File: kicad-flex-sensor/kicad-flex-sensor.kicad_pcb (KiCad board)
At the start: 2 copper layers, 68.6 x 53.3 mm, 8 parts, among them J1 Power, J2 Digital/PWM, J3 Analog, J4 Digital/PWM

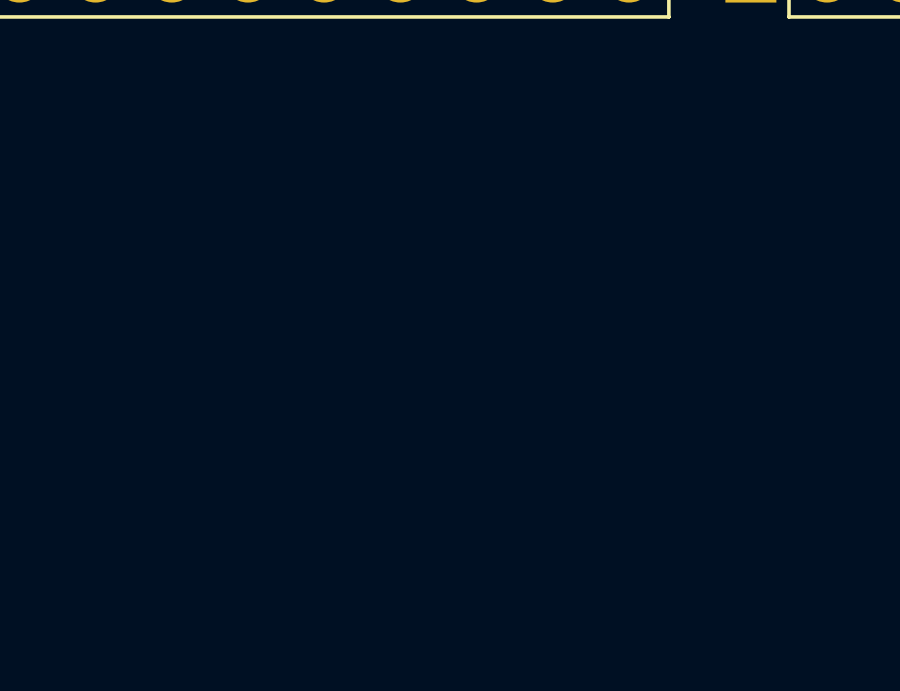
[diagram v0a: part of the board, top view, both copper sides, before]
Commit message: add bluetooth symbol and footprint
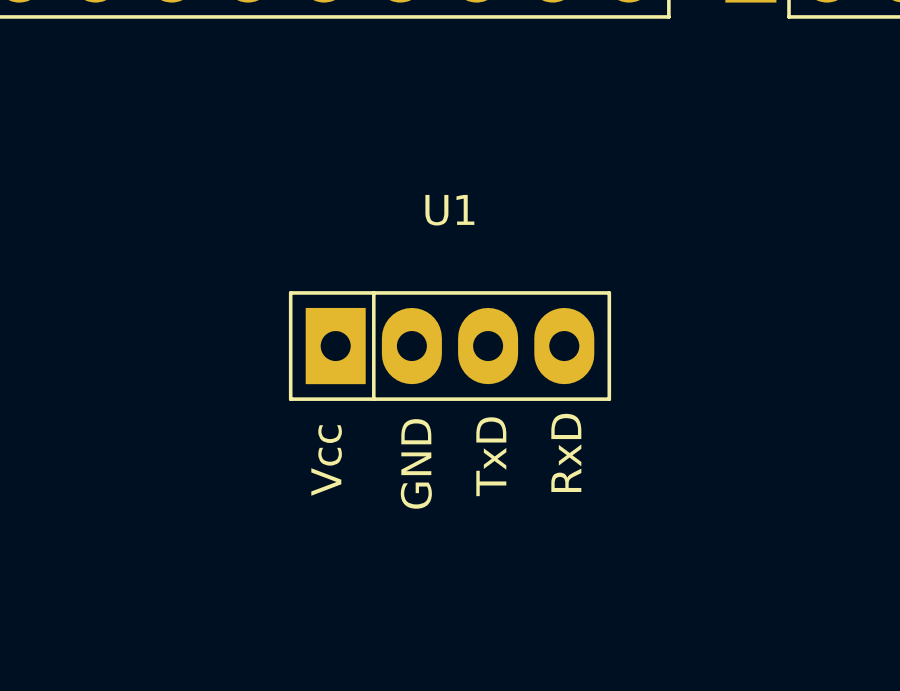
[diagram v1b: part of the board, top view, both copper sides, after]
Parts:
- added U1: ~, graphite_empreinte:Bluetooth_empreinte, F.Cu at (135.7, 61.5)
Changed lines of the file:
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@@
 	(net 29 "/SCL")
 	(net 30 "/SDA")
+	(net 31 "unconnected-(U1-GND-Pad2)")
+	(net 32 "unconnected-(U1-TxD-Pad3)")
+	(net 33 "unconnected-(U1-Vcc-Pad1)")
+	(net 34 "unconnected-(U1-RxD-Pad4)")
 	(footprint "Connector_PinSocket_2.54mm:PinSocket_1x08_P2.54mm_Vertical"
 		(locked yes)
@@
 		)
 		(embedded_fonts no)
+	)
+	(footprint "graphite_empreinte:Bluetooth_empreinte"
+		(layer "F.Cu")
+		(at 135.69 61.5)
+		(property "Reference" "U1"
+			(at 0 -4.5 0)
+			(layer "F.SilkS")
+			(effects
+				(font
+					(size 1 1)
+					(thickness 0.15)
+				)
+			)
+		)
+		(property "Value" "~"
+			(at 0 -2.77 0)
+			(layer "F.Fab")
+			(effects
+				(font
+					(size 1 1)
+					(thickness 0.15)
+				)
+			)
+		)
+		(property "Datasheet" ""
+			(at 0 0 0)
+			(layer "F.Fab")
+			(hide yes)
+			(effects
+				(font
+					(size 1.27 1.27)
+					(thickness 0.15)
+				)
+			)
+		)
+		(property "Description" ""
+			(at 0 0 0)
+			(layer "F.Fab")
+			(hide yes)
+			(effects
+				(font
+					(size 1.27 1.27)
+					(thickness 0.15)
+				)
+			)
+		)
+		(sheetname "/")
+		(sheetfile "kicad-flex-sensor.kicad_sch")
+		(attr through_hole)
+		(fp_line
+			(start -5.31 -1.77)
+			(end 5.31 -1.77)
+			(stroke
+				(width 0.12)
+				(type default)
+			)
+			(layer "F.SilkS")
+		)
+		(fp_line
+			(start -5.31 1.77)
+			(end -5.31 -1.77)
+			(stroke
+				(width 0.12)
+				(type default)
+			)
+			(layer "F.SilkS")
+		)
+		(fp_line
+			(start -2.54 -1.77)
+			(end -2.54 1.77)
+			(stroke
+				(width 0.12)
+				(type default)
+			)
+			(layer "F.SilkS")
+		)
+		(fp_line
+			(start 5.31 -1.77)
+			(end 5.31 1.77)
+			(stroke
+				(width 0.12)
+				(type default)
+			)
+			(layer "F.SilkS")
+		)
+		(fp_line
+			(start 5.31 1.77)
+			(end -5.31 1.77)
+			(stroke
+				(width 0.12)
+				(type default)
+			)
+			(layer "F.SilkS")
+		)
+		(fp_line
+			(start -5.06 -1.52)
+			(end 5.06 -1.52)
+			(stroke
+				(width 0.05)
+				(type default)
+			)
+			(layer "F.CrtYd")
+		)
+		(fp_line
+			(start -5.06 1.52)
+			(end -5.06 -1.52)
+			(stroke
+				(width 0.05)
+				(type default)
+			)
+			(layer "F.CrtYd")
+		)
+		(fp_line
+			(start 5.06 -1.52)
+			(end 5.06 1.52)
+			(stroke
+				(width 0.05)
+				(type default)
+			)
+			(layer "F.CrtYd")
+		)
+		(fp_line
+			(start 5.06 1.52)
+			(end -5.06 1.52)
+			(stroke
+				(width 0.05)
+				(type default)
+			)
+			(layer "F.CrtYd")
+		)
+		(fp_text user "RxD"
+			(at 4.5 5 90)
+			(unlocked yes)
+			(layer "F.SilkS")
+			(effects
+				(font
+					(size 1 1)
+					(thickness 0.1)
+				)
+				(justify left bottom)
+			)
+		)
+		(fp_text user "Vcc"
+			(at -3.5 5 90)
+			(unlocked yes)
+			(layer "F.SilkS")
+			(effects
+				(font
+					(size 1 1)
+					(thickness 0.1)
+				)
+				(justify left bottom)
+			)
+		)
+		(fp_text user "GND"
+			(at -0.5 5.5 90)
+			(unlocked yes)
+			(layer "F.SilkS")
+			(effects
+				(font
+					(size 1 1)
+					(thickness 0.1)
+				)
+				(justify left bottom)
+			)
+		)
+		(fp_text user "TxD"
+			(at 2 5 90)
+			(unlocked yes)
+			(layer "F.SilkS")
+			(effects
+				(font
+					(size 1 1)
+					(thickness 0.1)
+				)
+				(justify left bottom)
+			)
+		)
+		(pad "1" thru_hole rect
+			(at -3.81 0)
+			(size 2 2.54)
+			(drill 1)
+			(layers "*.Cu" "*.Mask")
+			(remove_unused_layers no)
+			(net 33 "unconnected-(U1-Vcc-Pad1)")
+			(pinfunction "Vcc")
+			(pintype "input")
+			(thermal_bridge_angle 45)
+		)
+		(pad "2" thru_hole oval
+			(at -1.27 0)
+			(size 2 2.54)
+			(drill 1)
+			(layers "*.Cu" "*.Mask")
+			(remove_unused_layers no)
+			(net 31 "unconnected-(U1-GND-Pad2)")
+			(pinfunction "GND")
+			(pintype "input")
+			(thermal_bridge_angle 45)
+		)
+		(pad "3" thru_hole oval
+			(at 1.27 0)
+			(size 2 2.54)
+			(drill 1)
+			(layers "*.Cu" "*.Mask")
+			(remove_unused_layers no)
+			(net 32 "unconnected-(U1-TxD-Pad3)")
+			(pinfunction "TxD")
+			(pintype "input")
+			(thermal_bridge_angle 45)
+		)
+		(pad "4" thru_hole oval
+			(at 3.81 0)
+			(size 2 2.54)
+			(drill 1)
+			(layers "*.Cu" "*.Mask")
+			(remove_unused_layers no)
+			(net 34 "unconnected-(U1-RxD-Pad4)")
+			(pinfunction "RxD")
+			(pintype "input")
+			(thermal_bridge_angle 45)
+		)
+		(embedded_fonts no)
